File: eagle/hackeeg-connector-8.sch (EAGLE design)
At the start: 21 parts

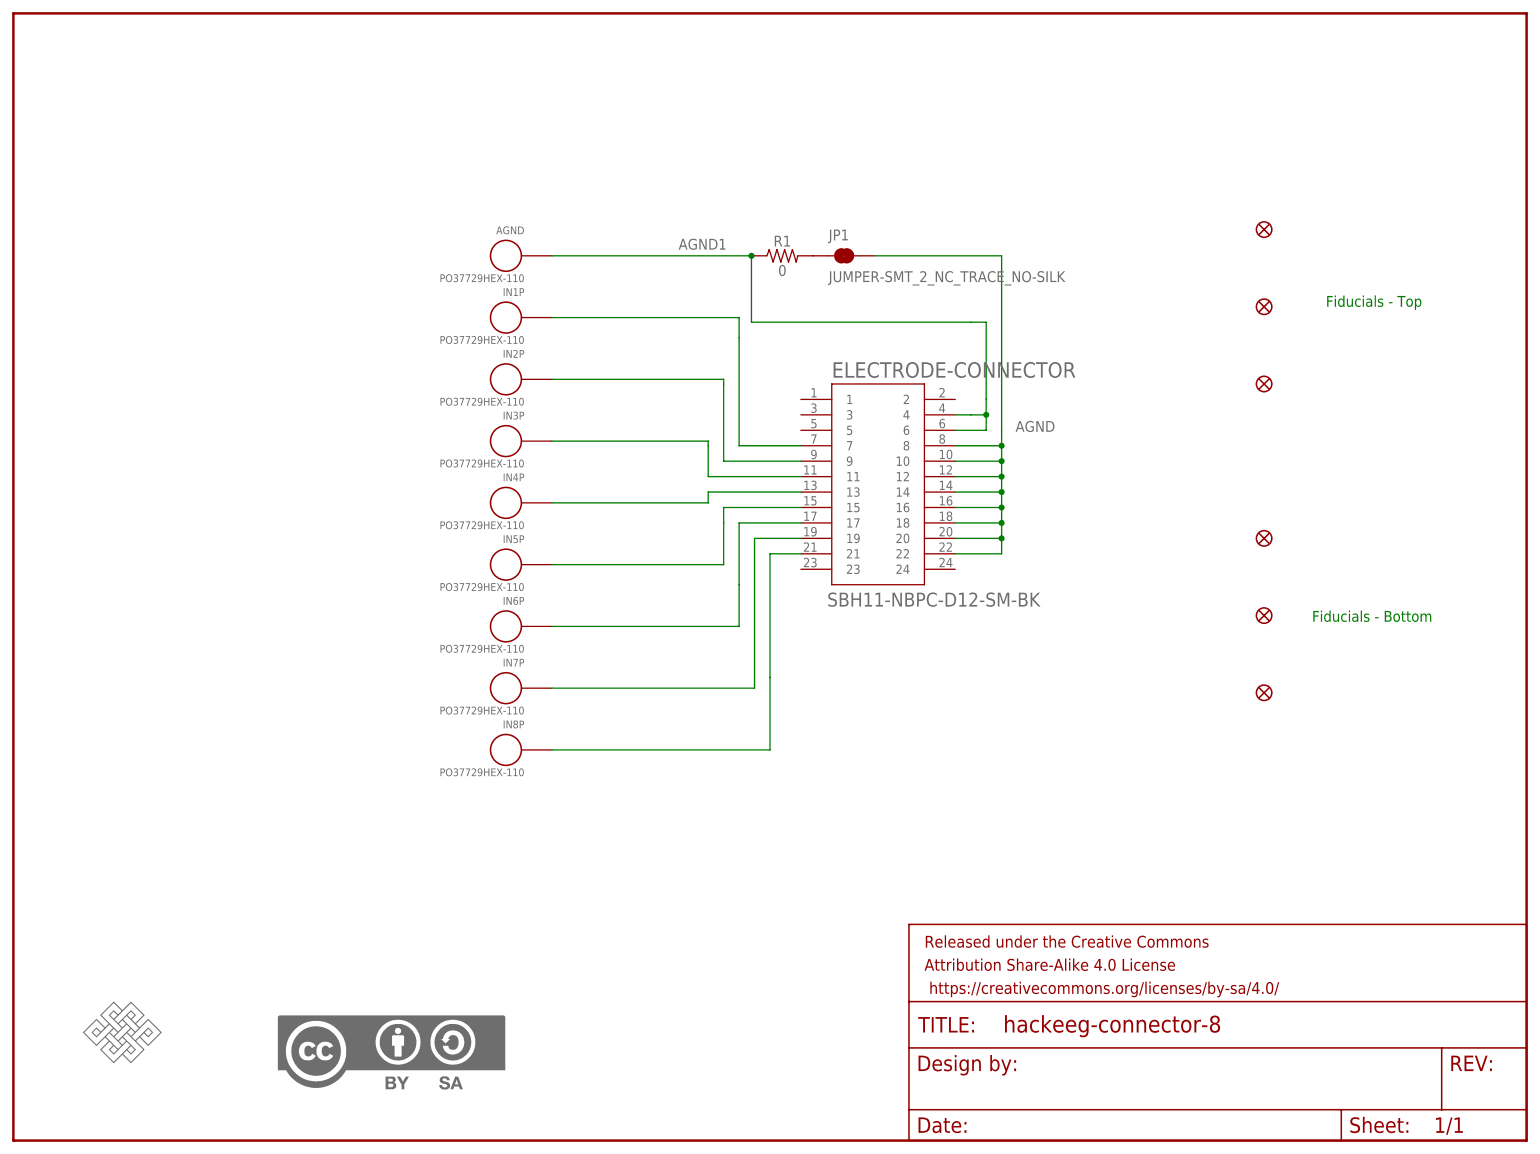
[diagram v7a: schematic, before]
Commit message: add connector version numbers to schematic and PCB
- also added board names to PCBs
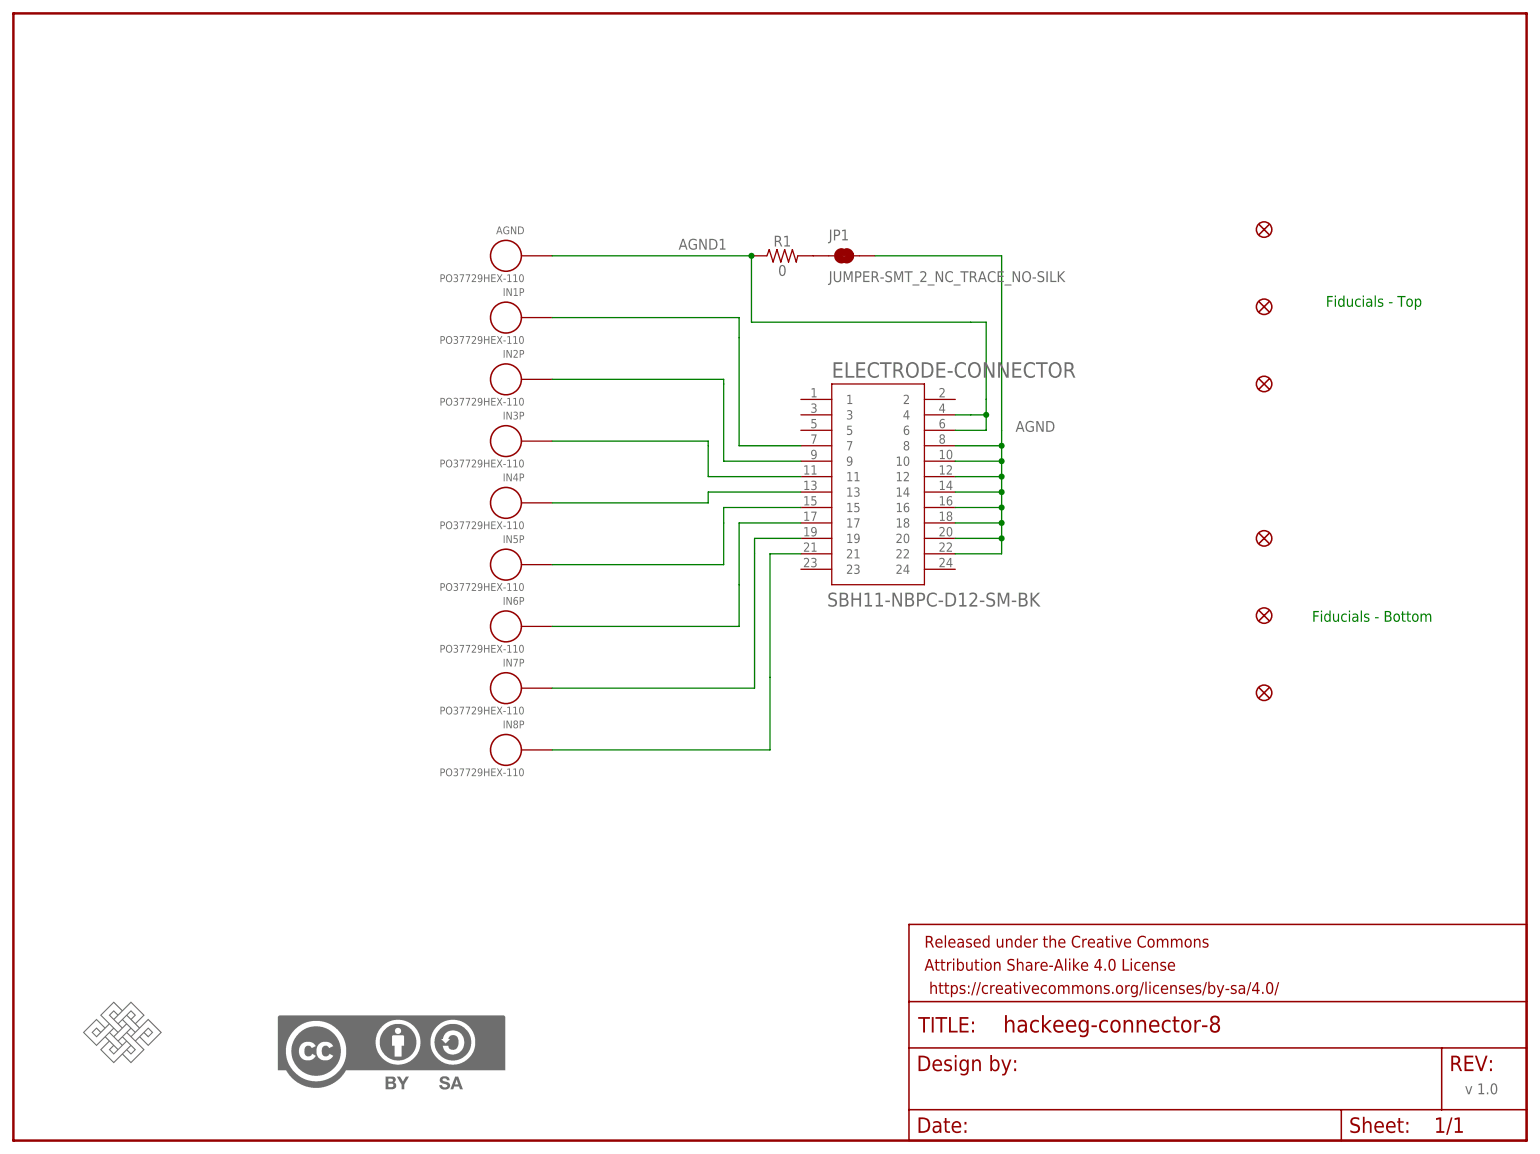
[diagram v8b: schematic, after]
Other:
- note added: "v 1.0"
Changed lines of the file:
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@@
 <?xml version="1.0" encoding="utf-8"?>
 <!DOCTYPE eagle SYSTEM "eagle.dtd">
-<eagle version="9.1.2">
+<eagle version="9.4.0">
 <drawing>
 <settings>
@@
 <text x="365.76" y="182.88" size="1.778" layer="91">Fiducials - Top</text>
 <text x="363.474" y="131.064" size="1.778" layer="91">Fiducials - Bottom</text>
+<text x="388.62" y="53.34" size="1.778" layer="95">v 1.0</text>
 </plain>
 <instances>
-<instance part="IN1P" gate="G$1" x="238.506" y="181.102" rot="MR0"/>
-<instance part="FRAME1" gate="G$1" x="149.86" y="45.72"/>
-<instance part="FRAME1" gate="V" x="297.18" y="45.72"/>
+<instance part="IN1P" gate="G$1" x="238.506" y="181.102" smashed="yes" rot="MR0">
+<attribute name="NAME" x="233.934" y="184.658" size="1.27" layer="95" rot="MR0"/>
+<attribute name="VALUE" x="233.934" y="176.784" size="1.27" layer="95" rot="MR0"/>
+</instance>
+<instance part="FRAME1" gate="G$1" x="149.86" y="45.72" smashed="yes"/>
+<instance part="FRAME1" gate="V" x="297.18" y="45.72" smashed="yes">
+<attribute name="LAST_DATE_TIME" x="309.88" y="46.99" size="2.54" layer="94" font="vector"/>
+<attribute name="SHEET" x="383.54" y="46.99" size="2.54" layer="94" font="vector"/>
+<attribute name="DRAWING_NAME" x="312.674" y="63.5" size="2.7432" layer="94" font="vector"/>
+</instance>
 <instance part="ELECTRODE-CONNECTOR" gate="G$1" x="292.1" y="152.4" smashed="yes">
 <attribute name="NAME" x="284.48" y="171.20891875" size="2.54646875" layer="95"/>
 <attribute name="VALUE" x="283.718" y="133.5629" size="2.28846875" layer="96"/>
 </instance>
-<instance part="U$13" gate="G$1" x="193.04" y="53.34"/>
-<instance part="IN2P" gate="G$1" x="238.506" y="170.942" rot="MR0"/>
-<instance part="IN3P" gate="G$1" x="238.506" y="160.782" rot="MR0"/>
-<instance part="IN4P" gate="G$1" x="238.506" y="150.622" rot="MR0"/>
-<instance part="IN5P" gate="G$1" x="238.506" y="140.462" rot="MR0"/>
-<instance part="IN6P" gate="G$1" x="238.506" y="130.302" rot="MR0"/>
-<instance part="IN7P" gate="G$1" x="238.506" y="120.142" rot="MR0"/>
-<instance part="AGND" gate="G$1" x="238.506" y="191.262" rot="MR0"/>
-<instance part="IN8P" gate="G$1" x="238.506" y="109.982" rot="MR0"/>
-<instance part="U$1" gate="G$1" x="167.64" y="63.5"/>
-<instance part="FD1" gate="G$1" x="355.6" y="170.18"/>
-<instance part="FD2" gate="G$1" x="355.6" y="182.88"/>
-<instance part="FD3" gate="G$1" x="355.6" y="195.58"/>
-<instance part="FD4" gate="G$1" x="355.6" y="144.78"/>
-<instance part="FD5" gate="G$1" x="355.6" y="132.08"/>
-<instance part="FD6" gate="G$1" x="355.6" y="119.38"/>
-<instance part="R1" gate="G$1" x="276.352" y="191.262"/>
-<instance part="JP1" gate="G$1" x="286.512" y="191.262"/>
+<instance part="U$13" gate="G$1" x="193.04" y="53.34" smashed="yes"/>
+<instance part="IN2P" gate="G$1" x="238.506" y="170.942" smashed="yes" rot="MR0">
+<attribute name="NAME" x="233.934" y="174.498" size="1.27" layer="95" rot="MR0"/>
+<attribute name="VALUE" x="233.934" y="166.624" size="1.27" layer="95" rot="MR0"/>
+</instance>
+<instance part="IN3P" gate="G$1" x="238.506" y="160.782" smashed="yes" rot="MR0">
+<attribute name="NAME" x="233.934" y="164.338" size="1.27" layer="95" rot="MR0"/>
+<attribute name="VALUE" x="233.934" y="156.464" size="1.27" layer="95" rot="MR0"/>
+</instance>
+<instance part="IN4P" gate="G$1" x="238.506" y="150.622" smashed="yes" rot="MR0">
+<attribute name="NAME" x="233.934" y="154.178" size="1.27" layer="95" rot="MR0"/>
+<attribute name="VALUE" x="233.934" y="146.304" size="1.27" layer="95" rot="MR0"/>
+</instance>
+<instance part="IN5P" gate="G$1" x="238.506" y="140.462" smashed="yes" rot="MR0">
+<attribute name="NAME" x="233.934" y="144.018" size="1.27" layer="95" rot="MR0"/>
+<attribute name="VALUE" x="233.934" y="136.144" size="1.27" layer="95" rot="MR0"/>
+</instance>
+<instance part="IN6P" gate="G$1" x="238.506" y="130.302" smashed="yes" rot="MR0">
+<attribute name="NAME" x="233.934" y="133.858" size="1.27" layer="95" rot="MR0"/>
+<attribute name="VALUE" x="233.934" y="125.984" size="1.27" layer="95" rot="MR0"/>
+</instance>
+<instance part="IN7P" gate="G$1" x="238.506" y="120.142" smashed="yes" rot="MR0">
+<attribute name="NAME" x="233.934" y="123.698" size="1.27" layer="95" rot="MR0"/>
+<attribute name="VALUE" x="233.934" y="115.824" size="1.27" layer="95" rot="MR0"/>
+</instance>
+<instance part="AGND" gate="G$1" x="238.506" y="191.262" smashed="yes" rot="MR0">
+<attribute name="NAME" x="233.934" y="194.818" size="1.27" layer="95" rot="MR0"/>
+<attribute name="VALUE" x="233.934" y="186.944" size="1.27" layer="95" rot="MR0"/>
+</instance>
+<instance part="IN8P" gate="G$1" x="238.506" y="109.982" smashed="yes" rot="MR0">
+<attribute name="NAME" x="233.934" y="113.538" size="1.27" layer="95" rot="MR0"/>
+<attribute name="VALUE" x="233.934" y="105.664" size="1.27" layer="95" rot="MR0"/>
+</instance>
+<instance part="U$1" gate="G$1" x="167.64" y="63.5" smashed="yes"/>
+<instance part="FD1" gate="G$1" x="355.6" y="170.18" smashed="yes"/>
+<instance part="FD2" gate="G$1" x="355.6" y="182.88" smashed="yes"/>
+<instance part="FD3" gate="G$1" x="355.6" y="195.58" smashed="yes"/>
+<instance part="FD4" gate="G$1" x="355.6" y="144.78" smashed="yes"/>
+<instance part="FD5" gate="G$1" x="355.6" y="132.08" smashed="yes"/>
+<instance part="FD6" gate="G$1" x="355.6" y="119.38" smashed="yes"/>
+<instance part="R1" gate="G$1" x="276.352" y="191.262" smashed="yes">
+<attribute name="NAME" x="276.352" y="192.786" size="1.778" layer="95" font="vector" align="bottom-center"/>
+<attribute name="VALUE" x="276.352" y="189.738" size="1.778" layer="96" font="vector" align="top-center"/>
+</instance>
+<instance part="JP1" gate="G$1" x="286.512" y="191.262" smashed="yes">
+<attribute name="NAME" x="283.972" y="193.802" size="1.778" layer="95" font="vector"/>
+<attribute name="VALUE" x="283.972" y="188.722" size="1.778" layer="96" font="vector" align="top-left"/>
+</instance>
 </instances>
 <busses>
